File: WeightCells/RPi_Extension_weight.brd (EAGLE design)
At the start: 63 x 50 mm, 23 parts, among them U1 AD7730BRUZ, U2 AD7730BRUZ, U3 AD7730BRUZ, U4 AD7730BRUZ, U5 AD7730BRUZ, U6 AD7730BRUZ, U7 AD7730BRUZ, U8 AD7730BRUZ, U9 STM32F103RCT6

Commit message: updated scale board
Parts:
- removed U3, U4, U5, U6, U7, U8: AD7730BRUZ, AD7730BRUZ:RU_24
- added C2, C3, C4, C5, C6: (no value), rcl:C0603
- added SV4: (no value), con-lstb:MA03-2
- moved U2 13.0 mm to (27.3, 18.9)
- moved U9 2.60 mm to (51.4, 31.2), flipped to the bottom
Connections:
- removed net PA7: U9.23
- removed net VDDA: U9.13
- removed net VDD_1: U9.32
- removed net VDD_2: U9.48
- removed net VDD_3: U9.64
- removed net VDD_4: U9.19
- new net N$2: SV1.1
- new net N$3: SV1.4
- new net N$4: SV1.3
- new net NRST: SV4.6, U9.7
- new net SPI1_MISO: U1.21, U2.21, U9.22
- new net SPI1_MOSI: U1.22, U2.22, U9.23
- new net SPI1_SCK: U1.1, U2.1, U9.21
- new net SS1: U1.19, U9.37
- new net SS2: U2.19, U9.38
- new net SS3: U9.39
- new net SS4: U9.40
- new net SS5: U9.41
- new net SS6: U9.42
- new net SS7: U9.43
- new net SS8: U9.44
- new net SS_STACK: SJ5.2, SJ6.2, SJ7.2, SJ8.2
- new net SWDCLK: SV4.3, U9.49
- new net SWDIO: SV4.4, U9.46
- new net U1_AIN1_+: SV1.16, U1.10
- new net U1_AIN1_-: SV1.15, U1.11
- new net U1_AIN2_+: SV1.14, U1.12
- new net U1_AIN2_-: SV1.13, U1.13
- new net U1_MCLK_OUT: U1.3, U2.2
- net +5V: now also U1.14, U2.9
- net DVCC: now also C2.2, C3.1, C4.1, C5.1, C6.1, SV4.1, U1.18, U1.5, U1.6, U2.23, U9.1, U9.13, U9.19, U9.32, U9.48, U9.64
- net GND: now also C2.1, C3.2, C4.2, C5.2, C6.2, SV4.2, SV4.5, U1.15, U1.4, U9.12, U9.18, U9.31, U9.47, U9.63; no longer SV1.10, SV1.12, SV1.14, SV1.16, SV1.2, SV1.4, SV1.6, SV1.8, SV2.10, SV2.12, SV2.14, SV2.16, SV2.2, SV2.4, SV2.6, SV2.8, U3.24, U3.8, U4.24, U4.8, U5.24, U5.8, U6.24, U6.8, U7.24, U7.8, U8.24, U8.8
- net SYNC: no longer SJ5.2, SJ6.2, SJ7.2, SJ8.2
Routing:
- net DVCC: track 40.7 -> 134.4 mm, vias 0 -> 3
- net SPI1_SCK: track 0.00 -> 45.1 mm, vias 0 -> 2
- net SS1: track 0.00 -> 35.5 mm, vias 0 -> 3
- net SPI1_MISO: track 0.00 -> 30.5 mm, vias 0 -> 2
- net SPI1_MOSI: track 0.00 -> 26.7 mm, vias 0 -> 2
- net SS2: track 0.00 -> 26.4 mm, vias 0 -> 1
- net U1_AIN1_+: track 0.00 -> 19.7 mm
- net SWDIO: track 0.00 -> 18.2 mm, vias 0 -> 1
- net U1_AIN2_+: track 0.00 -> 17.8 mm
- net NRST: track 0.00 -> 17.7 mm, vias 0 -> 1
- net U1_AIN1_-: track 0.00 -> 17.1 mm
- net U1_MCLK_OUT: track 0.00 -> 16.6 mm, vias 0 -> 2
- net SWDCLK: track 0.00 -> 16.5 mm
- net +5V: track 40.3 -> 56.8 mm, vias 1 -> 2
- net SYNC: track 41.1 -> 26.2 mm
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
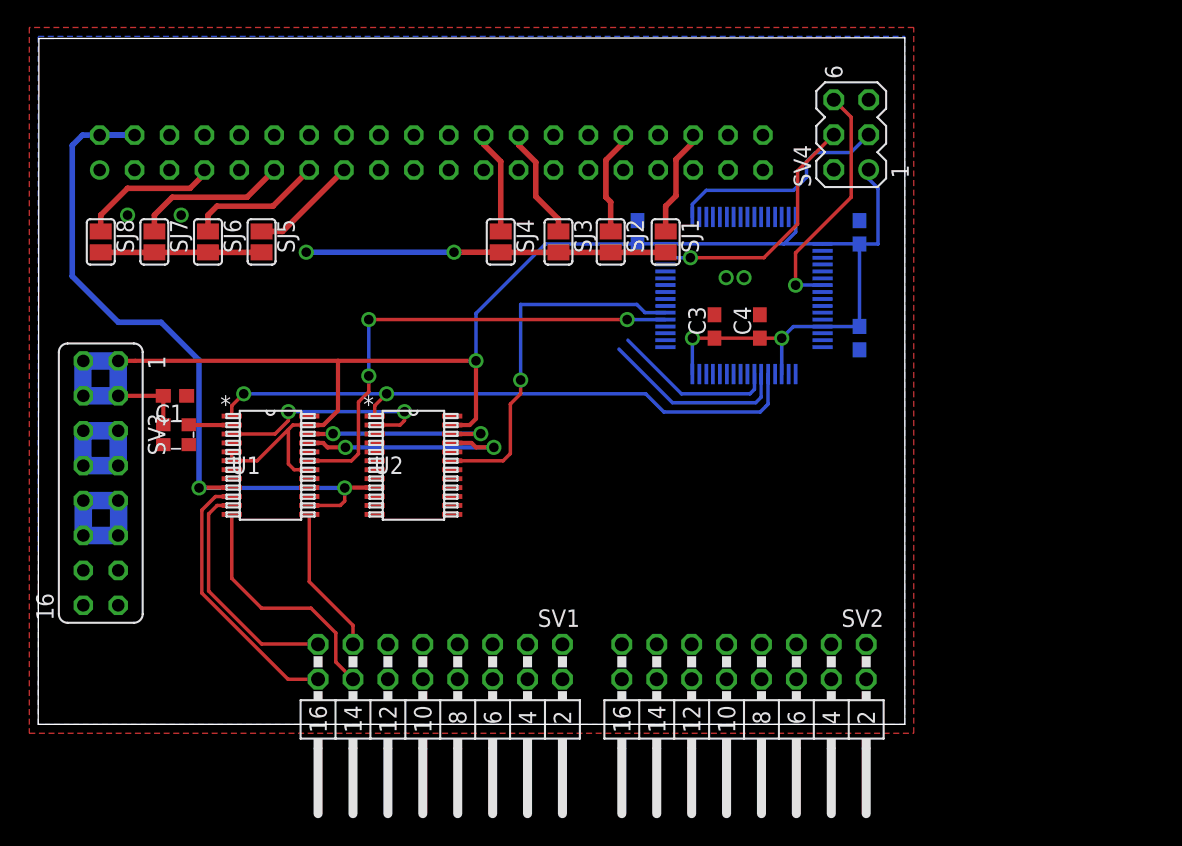
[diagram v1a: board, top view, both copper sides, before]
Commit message: finished top layer of scale board
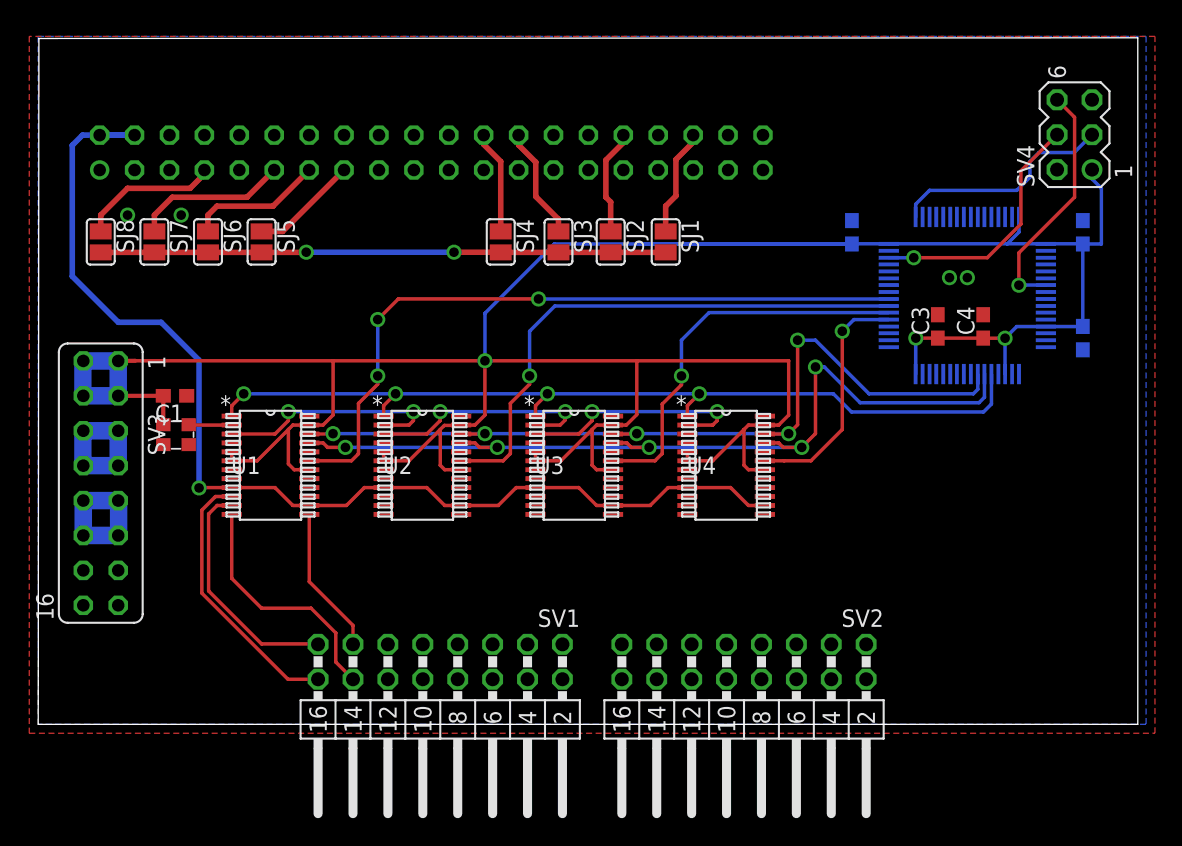
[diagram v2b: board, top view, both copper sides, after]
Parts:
- added U3, U4: AD7730BRUZ, AD7730BRUZ:RU_24
- moved SV4 16.3 mm to (75.4, 42.9)
- moved C2 16.2 mm to (76.0, 28.1)
- moved C3 16.2 mm to (65.5, 28.9)
- moved C4 16.2 mm to (68.8, 28.9)
- moved C6 16.2 mm to (76.0, 35.8)
- moved U9 16.2 mm to (67.6, 31.2)
- moved C5 15.6 mm to (59.2, 35.8)
- moved U2 0.65 mm to (27.9, 18.9)
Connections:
- removed net SYNC: SJ1.2, SJ2.2, SJ3.2, SJ4.2
- new net U2_MCLK_OUT: U2.3, U3.2
- new net U3_MCLK_OUT: U3.3, U4.2
- net +5V: now also U2.14, U3.14, U3.9, U4.14, U4.9
- net DVCC: now also U2.18, U2.5, U2.6, U3.18, U3.23, U3.5, U3.6, U4.18, U4.23, U4.5, U4.6
- net GND: now also U2.15, U2.4, U3.15, U3.24, U3.4, U3.8, U4.15, U4.24, U4.4, U4.8
- net SPI1_MISO: now also U3.21, U4.21
- net SPI1_MOSI: now also U3.22, U4.22
- net SPI1_SCK: now also U3.1, U4.1
- net SS1: now also U9.40; no longer U9.37
- net SS2: now also U9.39; no longer U9.38
- net SS3: now also U3.19, U9.38; no longer U9.39
- net SS4: now also U4.19, U9.37; no longer U9.40
- net SS_STACK: now also SJ1.2, SJ2.2, SJ3.2, SJ4.2
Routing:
- net DVCC: track 134.4 -> 250.4 mm
- net SPI1_MOSI: track 26.7 -> 63.2 mm, vias 2 -> 5
- net SPI1_MISO: track 30.5 -> 65.8 mm, vias 2 -> 5
- net SS_STACK: track 11.7 -> 41.1 mm, vias 0 -> 2
- net SS3: track 0.00 -> 28.5 mm, vias 0 -> 1
- net SYNC: track 26.2 -> 0.00 mm, vias 2 -> 0
- net +5V: track 56.8 -> 82.9 mm, vias 2 -> 1
- net SPI1_SCK: track 45.1 -> 65.3 mm, vias 2 -> 4
- net SS4: track 0.00 -> 17.5 mm, vias 0 -> 1
- net U3_MCLK_OUT: track 0.00 -> 17.2 mm, vias 0 -> 2
- net U2_MCLK_OUT: track 0.00 -> 17.2 mm, vias 0 -> 2
- net SS1: track 35.5 -> 51.9 mm
- net SS2: track 26.4 -> 40.2 mm
- net U1_MCLK_OUT: track 16.6 -> 17.2 mm
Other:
- board size 63 x 50 mm -> 80 x 50 mm

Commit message: finished top layer of scale board
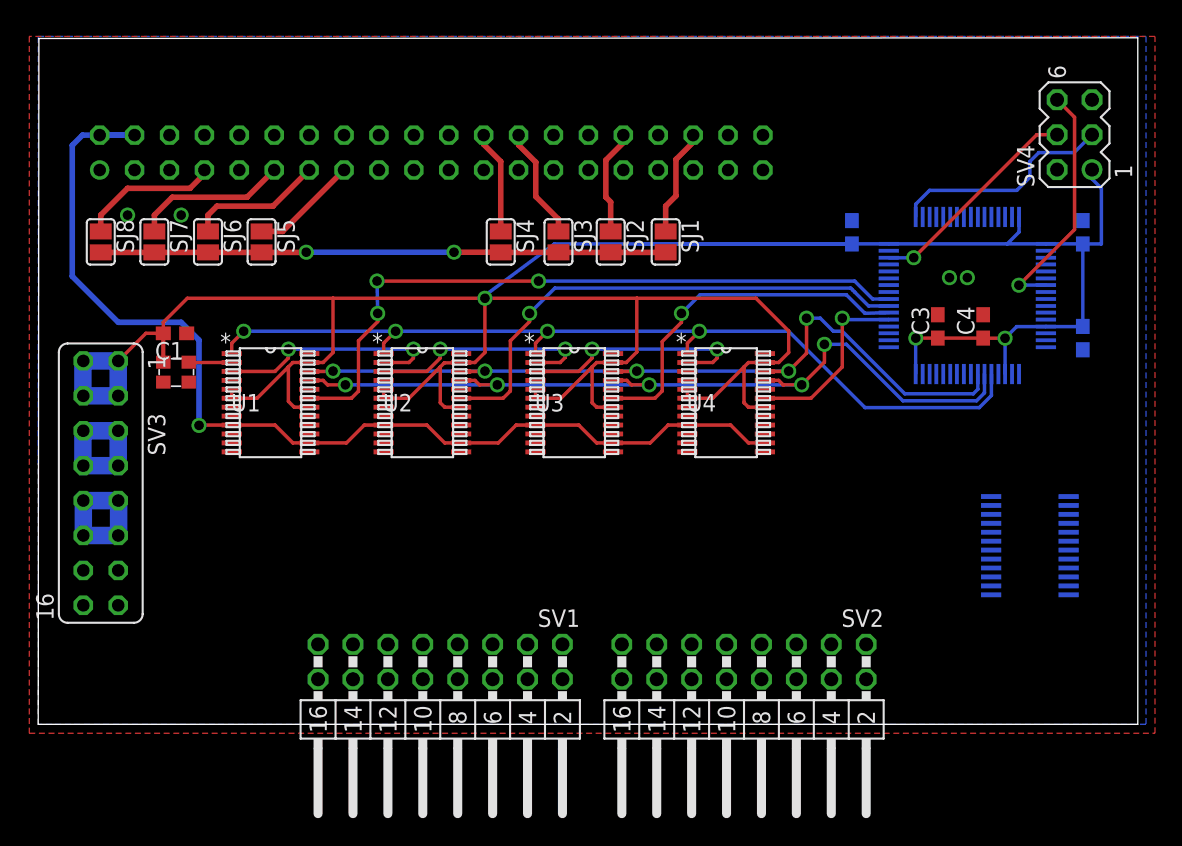
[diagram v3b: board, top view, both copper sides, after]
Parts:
- added U5: AD7730BRUZ, AD7730BRUZ:RU_24
- moved C1 4.55 mm to (9.95, 28.4)
- moved U$1 4.55 mm to (9.10, 26.4)
- moved U1 4.55 mm to (16.9, 23.4)
- moved U2 4.55 mm to (27.9, 23.4)
- moved U3 4.55 mm to (39.0, 23.4)
- moved U4 4.55 mm to (50.0, 23.4)
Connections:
- new net U4_MCLK_OUT: U4.3, U5.2
- net +5V: now also U5.14, U5.9
- net DVCC: now also U5.18, U5.23, U5.5, U5.6
- net GND: now also U5.15, U5.24, U5.4, U5.8
- net SPI1_MISO: now also U5.21
- net SPI1_MOSI: now also U5.22
- net SPI1_SCK: now also U5.1
- net SS5: now also U5.19
- net U1_AIN1_+: no longer U1.10
- net U1_AIN1_-: no longer U1.11
- net U1_AIN2_+: no longer U1.12
- net U1_AIN2_-: no longer U1.13
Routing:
- net U1_AIN1_+: track 19.7 -> 0.00 mm
- net U1_AIN2_+: track 17.8 -> 0.00 mm
- net U1_AIN1_-: track 17.1 -> 0.00 mm
- net U1_AIN2_-: track 10.8 -> 0.00 mm
- net DVCC: track 250.4 -> 244.0 mm
- net SS4: track 17.5 -> 13.6 mm
- net +5V: track 82.9 -> 79.2 mm
- net SPI1_MISO: track 65.8 -> 62.9 mm
- net SS2: track 40.2 -> 37.5 mm
- net SPI1_MOSI: track 63.2 -> 60.5 mm
- net SS3: track 28.5 -> 26.2 mm
- net SWDIO: track 18.2 -> 16.0 mm
- net SS1: track 51.9 -> 50.2 mm
- net SPI1_SCK: track 65.3 -> 66.6 mm

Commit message: added small design improvements
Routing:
- net DVCC: track 244.0 -> 255.6 mm
- net +5V: track 79.2 -> 85.4 mm
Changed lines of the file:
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@@
 <contactref element="U5" pad="4"/>
 <contactref element="U5" pad="15"/>
+<via x="20.15" y="29.9" extent="1-16" drill="0.7"/>
+<via x="22.75" y="29.9" extent="1-16" drill="0.7"/>
+<via x="31.2" y="29.9" extent="1-16" drill="0.7"/>
+<via x="33.8" y="29.9" extent="1-16" drill="0.7"/>
+<via x="42.25" y="29.9" extent="1-16" drill="0.7"/>
+<via x="44.85" y="29.9" extent="1-16" drill="0.7"/>
+<via x="51.35" y="29.9" extent="1-16" drill="0.7"/>
 </signal>
 <signal name="DVCC">
@@
 <contactref element="U5" pad="6"/>
 <contactref element="U5" pad="18"/>
-<wire x1="74.9694" y1="13.325" x2="74.9694" y2="13.975003125" width="0" layer="19" extent="16-16"/>
-<wire x1="69.3306" y1="12.675" x2="74.9694" y2="13.325" width="0" layer="19" extent="16-16"/>
-<wire x1="69.3306" y1="15.924996875" x2="69.3306" y2="12.675" width="0" layer="19" extent="16-16"/>
-<wire x1="70.3432" y1="25.485" x2="69.3306" y2="15.924996875" width="0" layer="19" extent="16-16"/>
+<wire x1="69.3306" y1="12.675" x2="70.525" y2="12.675" width="0.254" layer="16"/>
+<wire x1="70.525" y1="12.675" x2="70.85" y2="13" width="0.254" layer="16"/>
+<wire x1="70.85" y1="13" x2="70.85" y2="15.6" width="0.254" layer="16"/>
+<wire x1="69.3306" y1="15.924996875" x2="70.525003125" y2="15.924996875" width="0.254" layer="16"/>
+<wire x1="70.525003125" y1="15.924996875" x2="70.85" y2="15.6" width="0.254" layer="16"/>
+<wire x1="74.9694" y1="13.325" x2="73.125" y2="13.325" width="0.254" layer="16"/>
+<wire x1="73.125" y1="13.325" x2="70.85" y2="15.6" width="0.254" layer="16"/>
+<wire x1="74.9694" y1="13.975003125" x2="74.9694" y2="13.325" width="0.254" layer="16"/>
+<wire x1="70.3432" y1="25.485" x2="70.525003125" y2="15.924996875" width="0" layer="19" extent="16-16"/>
 </signal>
 <signal name="MISO">
@@
 <contactref element="U5" pad="9"/>
 <contactref element="U5" pad="14"/>
-<wire x1="69.3306" y1="10.075" x2="74.9694" y2="11.375003125" width="0" layer="19" extent="16-16"/>
+<wire x1="74.9694" y1="11.375003125" x2="71.825003125" y2="11.375003125" width="0.254" layer="16"/>
+<wire x1="71.825003125" y1="11.375003125" x2="70.525" y2="10.075" width="0.254" layer="16"/>
+<wire x1="69.3306" y1="10.075" x2="70.525" y2="10.075" width="0.254" layer="16"/>
 <wire x1="52.8694" y1="20.475" x2="69.3306" y2="10.075" width="0" layer="19" extent="1-16"/>
 </signal>

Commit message: updated design
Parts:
- moved C5 1.95 mm to (61.1, 35.8), flipped to the top
- moved C2 1.30 mm to (77.3, 28.1), flipped to the top
- moved C6 1.30 mm to (77.3, 35.8), flipped to the top
- moved C3 0.45 mm to (65.9, 28.9)
- moved C4 0.20 mm to (68.5, 28.9)
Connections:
- net N$2 renamed U4_AIN2_-
- net N$3 renamed U4_AIN1_+
- net N$4 renamed U4_AIN1_-
- new net N$1: U1.11
- new net N$10: U3.10
- new net N$11: U3.12
- new net N$12: U3.13
- new net N$13: U4.11
- new net N$14: U4.10
- new net N$15: U4.12
- new net N$16: U4.13
- new net N$2: U1.10
- new net N$3: U1.12
- new net N$4: U1.13
- new net N$5: U2.11
- new net N$6: U2.10
- new net N$7: U2.12
- new net N$8: U2.13
- new net N$9: U3.11
- new net U2_AIN1_+: SV1.12
- new net U2_AIN1_-: SV1.11
- new net U2_AIN2_+: SV1.10
- new net U2_AIN2_-: SV1.9
- new net U3_AIN1_+: SV1.8
- new net U3_AIN1_-: SV1.7
- new net U3_AIN2_+: SV1.6
- new net U3_AIN2_-: SV1.5
- new net U4_AIN2_+: SV1.2
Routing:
- net DVCC: track 255.6 -> 209.1 mm, vias 3 -> 5
- net U4_MCLK_OUT: track 0.00 -> 40.6 mm, vias 0 -> 1
- net +5V: track 85.4 -> 114.6 mm, vias 1 -> 2
- net SS1: track 50.2 -> 48.7 mm, vias 3 -> 1
- net SS_STACK: vias 2 -> 0

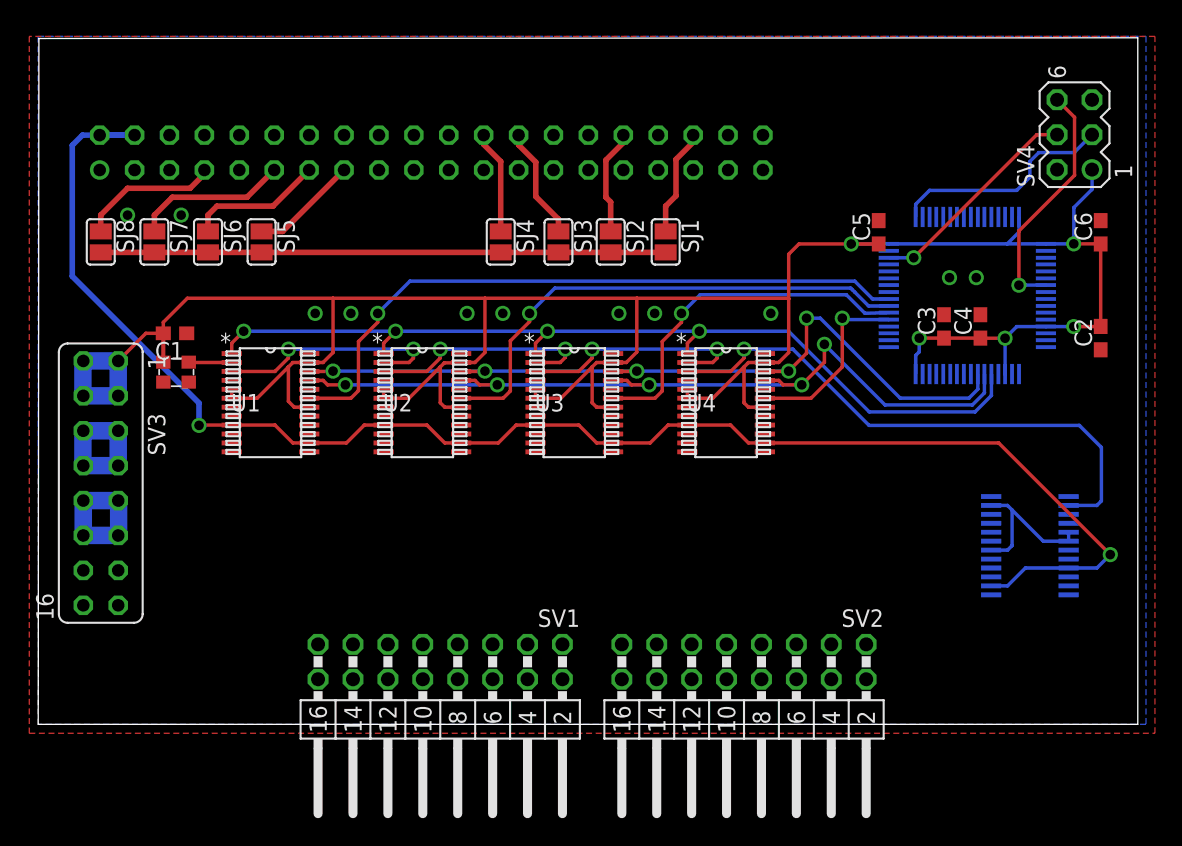
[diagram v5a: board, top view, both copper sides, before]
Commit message: added second set of transducers
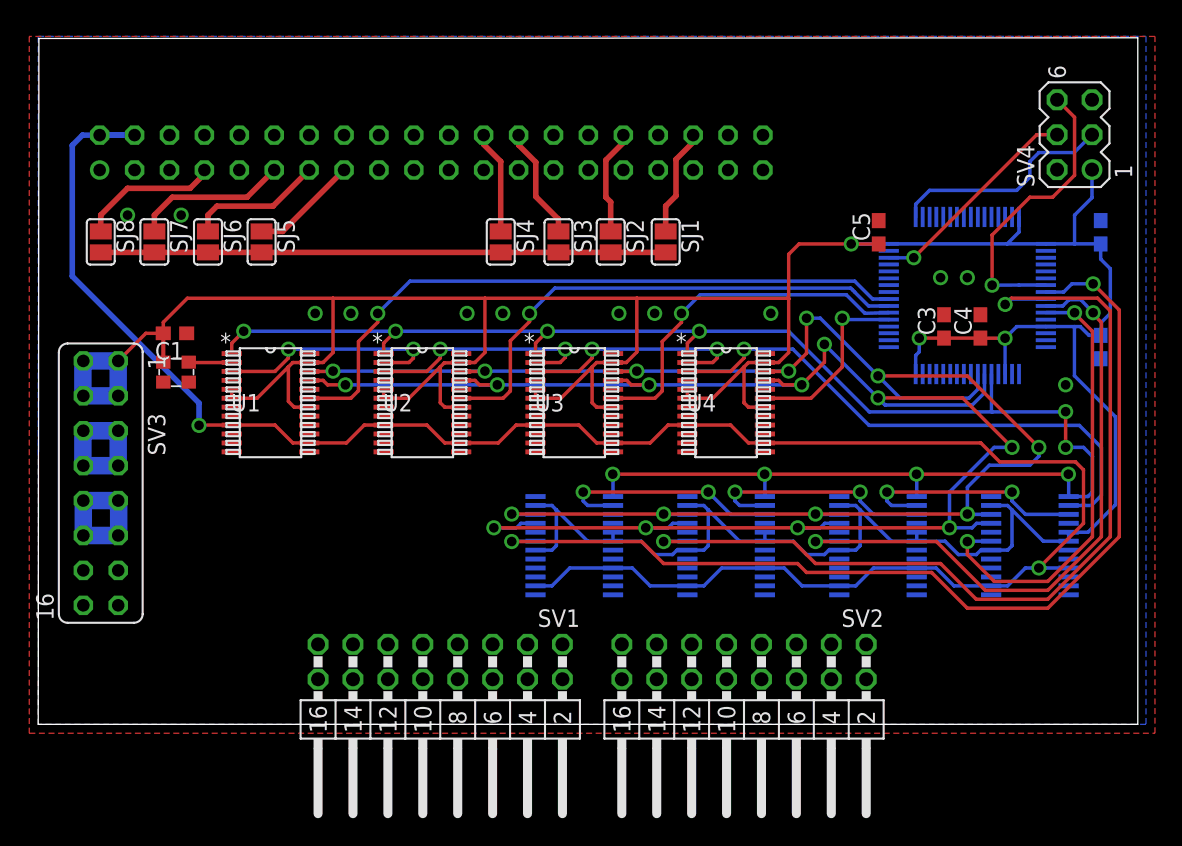
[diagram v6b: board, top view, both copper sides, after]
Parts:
- added U6, U7, U8: AD7730BRUZ, AD7730BRUZ:RU_24
- moved C2 0.65 mm to (77.3, 27.4), flipped to the bottom
- flipped C6 to the bottom
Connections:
- new net U5_MCLK_OUT: U5.3, U6.2
- new net U6_MCLK_OUT: U6.3, U7.2
- new net U7_MCLK_OUT: U7.3, U8.2
- net +5V: now also U6.14, U6.9, U7.14, U7.9, U8.14, U8.9
- net DVCC: now also U6.18, U6.23, U6.5, U6.6, U7.18, U7.23, U7.5, U7.6, U8.18, U8.23, U8.5, U8.6
- net GND: now also U6.15, U6.24, U6.4, U6.8, U7.15, U7.24, U7.4, U7.8, U8.15, U8.24, U8.4, U8.8
- net SPI1_MISO: now also U6.21, U7.21, U8.21
- net SPI1_MOSI: now also U6.22, U7.22, U8.22
- net SPI1_SCK: now also U6.1, U7.1, U8.1
- net SS5: now also U9.11; no longer U9.41
- net SS6: now also U6.19, U9.10; no longer U9.42
- net SS7: now also U7.19, U9.9; no longer U9.43
- net SS8: now also U8.19, U9.8; no longer U9.44
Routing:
- net SS8: track 0.00 -> 73.0 mm, vias 0 -> 2
- net DVCC: track 209.1 -> 281.8 mm, vias 5 -> 3
- net SPI1_MISO: track 63.1 -> 129.4 mm, vias 5 -> 11
- net SS7: track 0.00 -> 65.6 mm, vias 0 -> 2
- net SPI1_MOSI: track 60.7 -> 123.4 mm, vias 5 -> 11
- net SPI1_SCK: track 66.8 -> 121.9 mm, vias 4 -> 10
- net SS6: track 0.00 -> 46.2 mm, vias 0 -> 2
- net +5V: track 114.6 -> 151.6 mm
- net SS5: track 0.00 -> 33.2 mm, vias 0 -> 2
- net U6_MCLK_OUT: track 0.00 -> 17.2 mm, vias 0 -> 2
- net U5_MCLK_OUT: track 0.00 -> 17.2 mm, vias 0 -> 2
- net U7_MCLK_OUT: track 0.00 -> 16.8 mm, vias 0 -> 2
- net NRST: track 17.7 -> 21.4 mm
